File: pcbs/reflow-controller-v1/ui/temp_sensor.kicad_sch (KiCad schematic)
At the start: 7 parts, among them J1201 EB163A-04-C-180, U1201 MAX31865ATP+

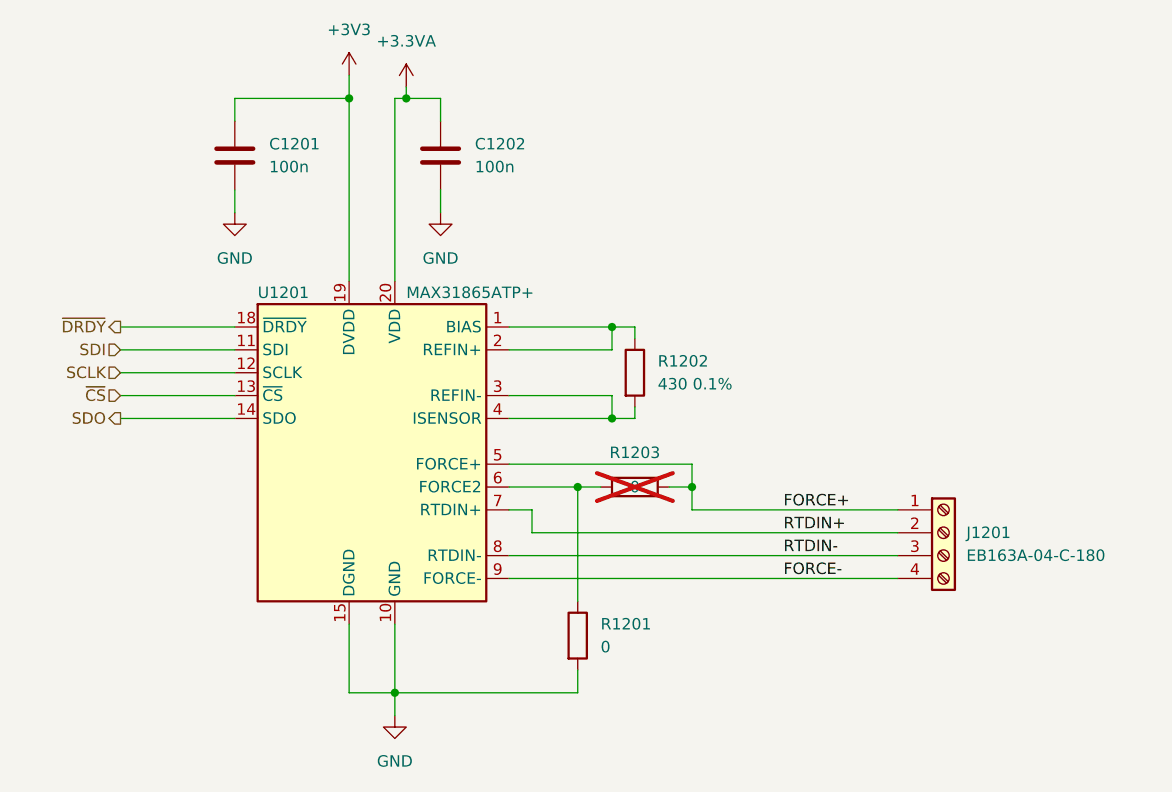
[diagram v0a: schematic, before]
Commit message: split pcbs into two for safety
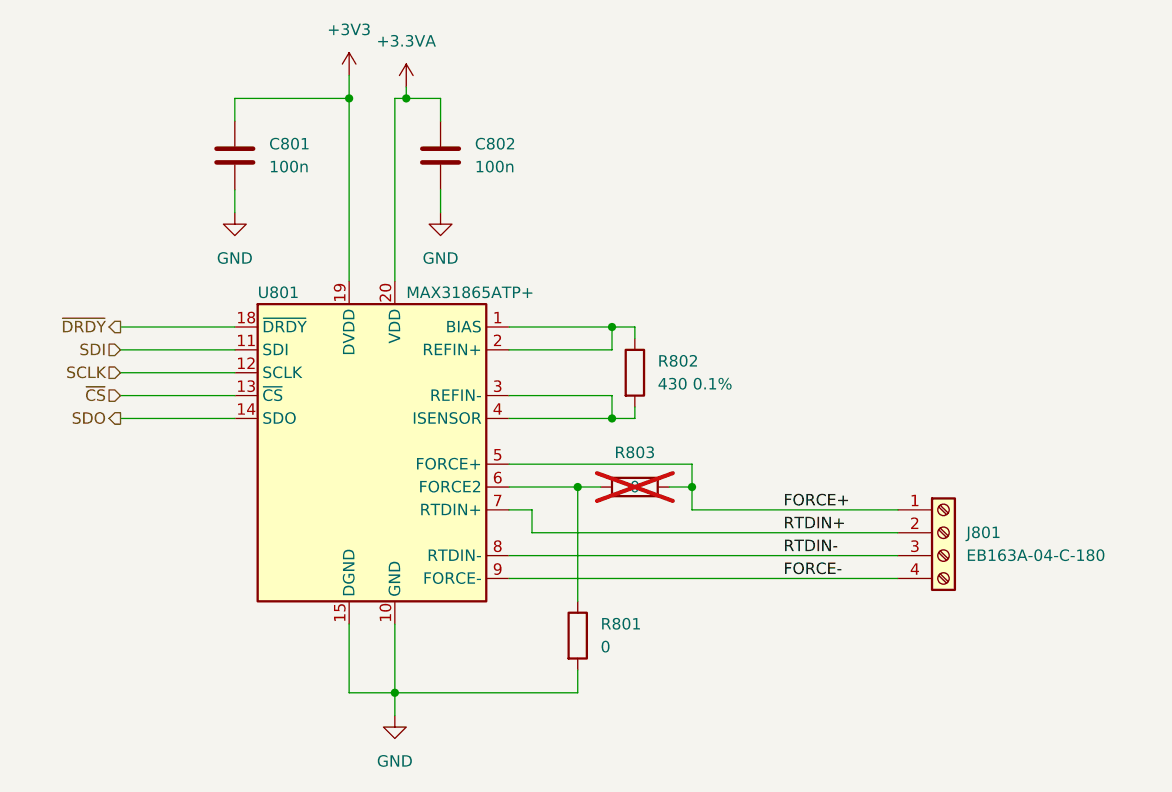
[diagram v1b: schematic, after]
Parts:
- renumbered C1201 to C801, C1202 to C802, J1201 to J801, R1201 to R801, R1202 to R802, R1203 to R803, U1201 to U801
